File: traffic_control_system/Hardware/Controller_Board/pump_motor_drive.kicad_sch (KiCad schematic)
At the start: 31 parts, among them J1 Screw_Terminal_01x03, Q17 2N3904, U24 74LVC1G04, U25 74LVC1G08, U26 VOL617A-7X001T

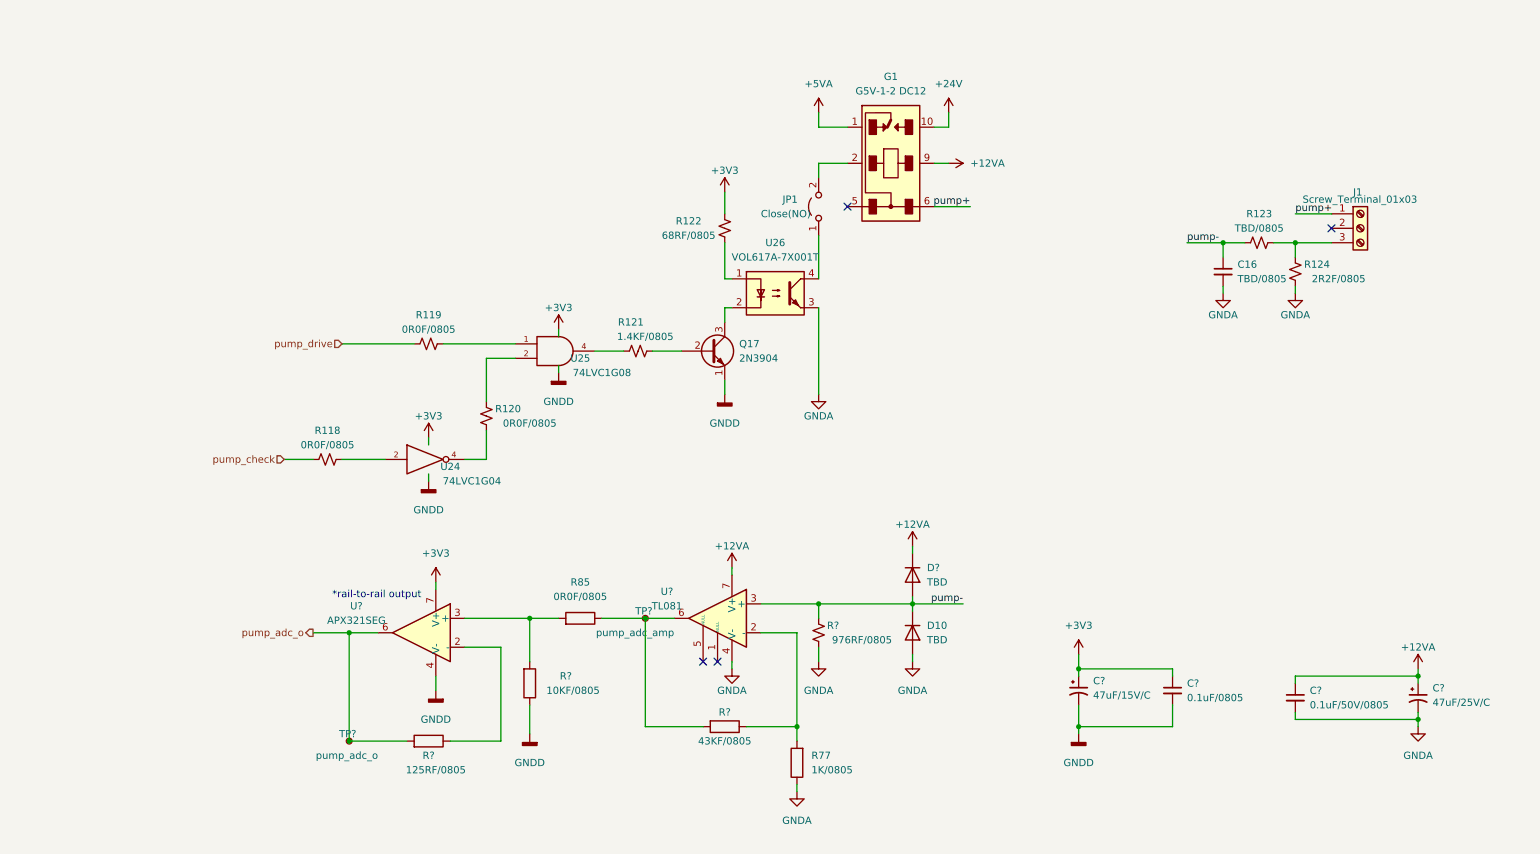
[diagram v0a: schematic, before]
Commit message: issue : 깃 커밋 히스토리 정리를 위한 원본 저장소의 브랜치 분리 작업[TRAFFIC-CONTROL6]
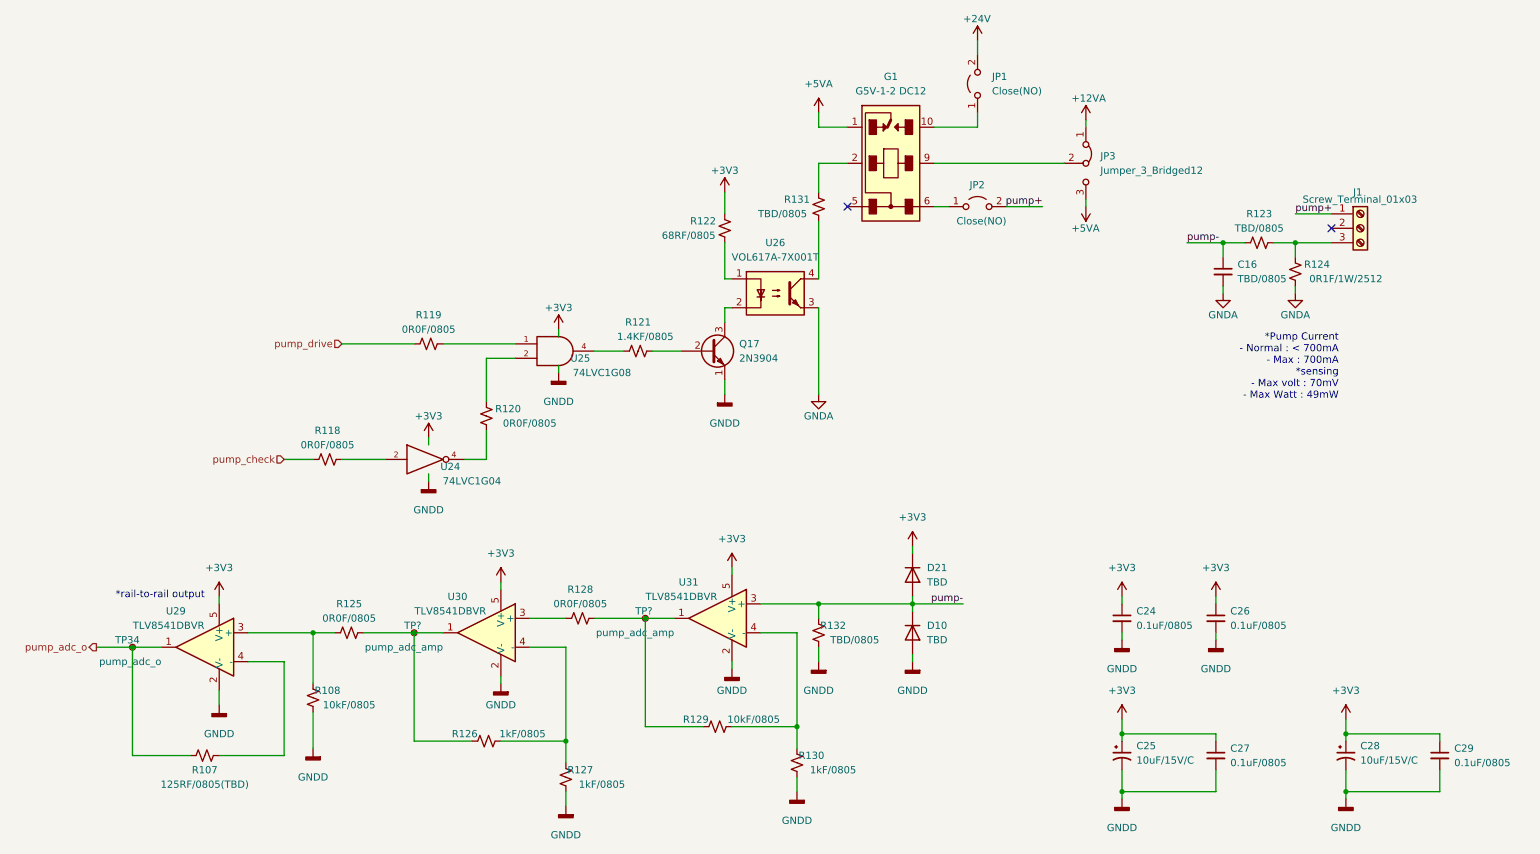
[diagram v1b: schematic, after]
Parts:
- removed C?: 0.1uF/50V/0805, symbol Device:C_Small
- removed C?: 47uF/25V/C, symbol Device:C_Polarized_Small_US
- removed R77: 1KF/0805, symbol Device:R
- removed R85: R, symbol Device:R
- removed R?: 125RF/0805, symbol Device:R
- removed R?: 43KF/0805, symbol Device:R
- removed R?: 10KF/0805, symbol Device:R
- removed TP?: pump_adc_o, symbol Connector:TestPoint_Small
- removed U?: APX321SEG, Package_SO:SOIC-8_3.9x4.9mm_P1.27mm, symbol Amplifier_Operational:OPA196xD
- removed U?: TL081, symbol Amplifier_Operational:TL081
- added C24, C26, C29: 0.1uF/0805, symbol Device:C_Small
- added C28: 10uF/15V/C, symbol Device:C_Polarized_Small_US
- added JP2: Close(NO), symbol Jumper:Jumper_2_Open
- added JP3: Jumper_3_Bridged12, symbol Jumper:Jumper_3_Bridged12
- added R107: 125RF/0805(TBD), symbol Device:R_Small_US
- added R108, R129: 10kF/0805, symbol Device:R_Small_US
- added R125, R128: 0R0F/0805, symbol Device:R_Small_US
- added R126, R127, R130: 1kF/0805, symbol Device:R_Small_US
- added R131: TBD/0805, symbol Device:R_Small_US
- added TP34: pump_adc_o, symbol Connector:TestPoint_Small
- added TP?: vavle_adc1, symbol Connector:TestPoint_Small
- added U29, U30, U31: TLV8541DBVR, Package_TO_SOT_SMD:SOT-23-5, symbol Amplifier_Operational:TLV2371DBV
- C25: renamed from C?; value 47uF/15V/C -> 10uF/15V/C
- R124: value 2R2F/0805 -> 0R1F/1W/2512; P/N (none) -> LR2512-22R010F4
- R132: renamed from R?; value 976RF/0805 -> TBD/0805
- gave numbers to parts that had none: 2
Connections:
- net +12VA: now also JP3.1 (A); no longer D21.1 (K), G1.9
- net +24V: now also JP1.2 (B); no longer G1.10
- net +3V3: now also D21.1 (K), C24.1, C26.1, C28.1, C29.1, U29.5 (V+), U30.5 (V+), U31.5 (V+)
- net +5VA: now also JP3.3 (B)
- net GND: now also D10.2 (A), R132.1, C24.2, C26.2, C28.2, C29.2, R108.1, R127.1, R130.1, U29.2 (V-), U30.2 (V-), U31.2 (V-)
- net GNDA: no longer D10.2 (A), R132.1
- net pump+: now also JP2.2 (B); no longer G1.6
- net pump-: now also U31.3 (+)
- net pump_adc_o: now also R107.1, TP34.1, U29.1
- net at TP?.1: now also R128.2, R129.1, U31.1
- net at G1.2: now also R131.1; no longer JP1.2 (B)
- net at JP1.1 (A): now also G1.10; no longer U26.4
- new net: R128.1, U30.3 (+)
- new net: R125.2, R126.1, TP?.1, U30.1
- new net: R126.2, R127.2, U30.4 (-)
- new net: R129.2, R130.2, U31.4 (-)
- new net: G1.9, JP3.2 (C)
- new net: R108.2, R125.1, U29.3 (+)
- new net: R107.2, U29.4 (-)
- new net: G1.6, JP2.1 (A)
- new net: R131.2, U26.4
- no-connect marks 4 -> 2
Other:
- note added: "*Pump Current - Normal : < 700mA - Max : 700mA *sensing - Max volt : 70mV - Max Watt : 49mW"
- moved on the sheet: C25, C27
